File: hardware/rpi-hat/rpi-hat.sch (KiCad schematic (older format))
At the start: 6 parts, among them P1 Conn_02x20_Odd_Even, U1 Telaire_6004_CO2

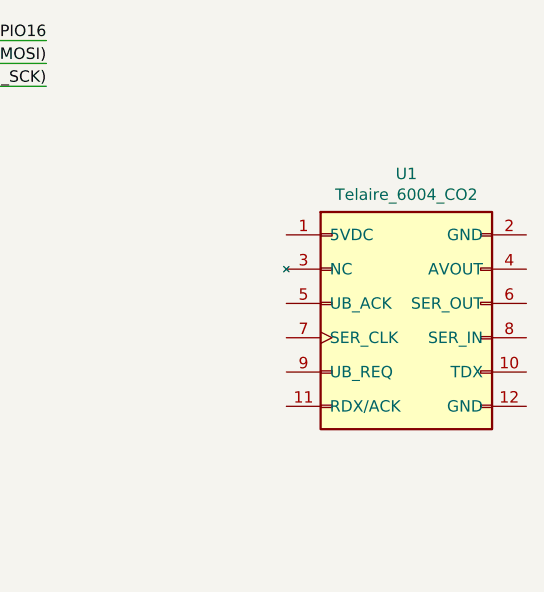
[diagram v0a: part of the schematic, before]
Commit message: Add KiCad Symbol for Sharp GP2Y1010.
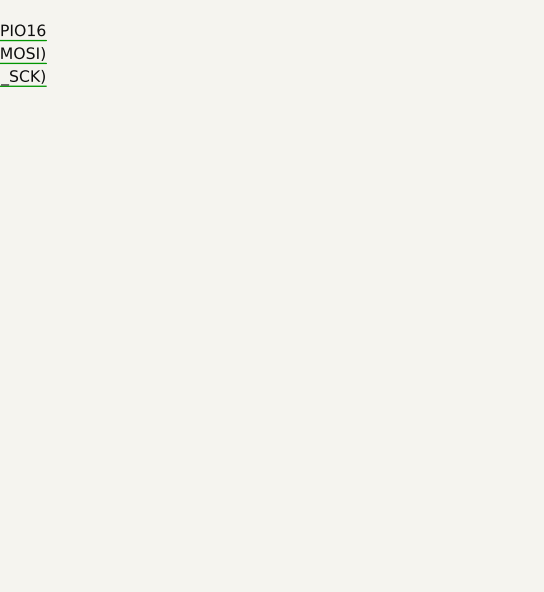
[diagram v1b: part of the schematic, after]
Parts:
- removed U1: Telaire_6004_CO2, symbol zephyrus_iaq:Telaire_6004_CO2
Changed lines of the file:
@@
 Wire Wire Line
 	3000 1700 3000 2000
-$Comp
-L zephyrus_iaq:Telaire_6004_CO2 U1
-U 1 1 5CB19ACF
-P 5150 3550
-F 0 "U1" H 5525 3717 50  0000 C CNN
-F 1 "Telaire_6004_CO2" H 5525 3626 50  0000 C CNN
-F 2 "" H 5700 2400 50  0001 C CNN
-F 3 "" H 5700 2400 50  0001 C CNN
-	1    5150 3550
-	1    0    0    -1
-$EndComp
 $EndSCHEMATC

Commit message: Most functionality added. EEPROM for HAT spec, various JST connectors for sensors, ADC subsystem and power subsystem
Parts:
- added C1: 47uF, Resistor_SMD:R_1206_3216Metric_Pad1.42x1.75mm_HandSolder, symbol Device:C
- added C2: 220uF, Resistor_SMD:R_0805_2012Metric_Pad1.15x1.40mm_HandSolder, symbol Device:CP1_Small
- added D1: SMBJ5.0A, Diode_SMD:D_SMB_Handsoldering, symbol Device:D_Schottky
- added F1: MF-MSMF250/X, Fuse:Fuse_1812_4532Metric, symbol Device:Polyfuse
- added J1: SM04B-SRSS-TB(LF)(SN), symbol zephyrus_iaq:SM04B-SRSS-TB(LF)(SN)
- added J10, J7, J9: S6B-ZR-SM4A-TF(LF)(SN)__Gas, symbol zephyrus_iaq:S6B-ZR-SM4A-TF(LF)(SN)__Gas
- added J2: Conn_01x02_Male, Connector_PinSocket_2.54mm:PinSocket_1x02_P2.54mm_Vertical, symbol Connector:Conn_01x02_Male
- added J3: 10103594-0001LF, 10103594-0001LF:FCI_10103594-0001LF, symbol zephyrus_iaq:10103594-0001LF
- added J4, J6, J8: SM04B-SRSS-TB(LF)(SN), SM04B-SRSS-TB_LF__SN_:JST_SM04B-SRSS-TB(LF)(SN), symbol zephyrus_iaq:SM04B-SRSS-TB(LF)(SN)
- added J5: S6B-ZR-SM4A-TF(LF)(SN)__Dust, symbol zephyrus_iaq:S6B-ZR-SM4A-TF(LF)(SN)__Dust
- added R1: R_US, symbol Device:R_US
- added R2, R3: 3.9k, Resistor_SMD:R_0805_2012Metric_Pad1.15x1.40mm_HandSolder, symbol Device:R_Small_US
- added R4: DNP, Resistor_SMD:R_0805_2012Metric_Pad1.15x1.40mm_HandSolder, symbol Device:R_Small_US
- added R5: 10k, Resistor_SMD:R_0805_2012Metric_Pad1.15x1.40mm_HandSolder, symbol Device:R_Small_US
- added R6: 150, Resistor_SMD:R_0805_2012Metric_Pad1.15x1.40mm_HandSolder, symbol Device:R_Small_US
- added R7: 1700, Resistor_SMD:R_0805_2012Metric_Pad1.15x1.40mm_HandSolder, symbol Device:R_US
- added R8: 3300, Resistor_SMD:R_0805_2012Metric_Pad1.15x1.40mm_HandSolder, symbol Device:R_US
- added U1: CAT24C32WI-GT3, CAT24C32WI-GT3:SOIC127P600X175-8N, symbol zephyrus_iaq:CAT24C32WI-GT3
- added U2: SN74LV4T125PWR, SN74LV4T125PWR:SOP65P640X120-14N, symbol zephyrus_iaq:SN74LV4T125PWR
- added U3: MCP3008T-I_SL, MCP3008T-I_SL:SOIC127P600X175-16N, symbol zephyrus_iaq:MCP3008T-I_SL
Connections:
- net GND is gone; now on net +5V: P1.14 (Pin_14), P1.20 (Pin_20), P1.25 (Pin_25), P1.30 (Pin_30), P1.34 (Pin_34), P1.39 (Pin_39), P1.6 (Pin_6), P1.9 (Pin_9)
- net +3V3: now also J4.3 (3.3V), J6.3 (3.3V), J8.3 (3.3V), R2.1, R3.1, R5.2, U1.8 (VCC)
- net +5V: now also C1.1, C1.2, C2.2, D1.1 (K), D1.2 (A), F1.1, J10.1 (VCC), J10.6 (GND), J2.2 (Pin_2), J3.5, J3.S3 (SHIELD), J3.S4 (SHIELD), J3.S5 (SHIELD), J3.S6 (SHIELD), J4.4 (GND), J5.2 (LED-GND), J5.4 (S-GND), J5.6 (Vcc), J6.4 (GND), J7.1 (VCC), J7.6 (GND), J8.4 (GND), J9.1 (VCC), J9.6 (GND), R4.1, R6.2, R8.2, U1.1 (A0), U1.2 (A1), U1.3 (A2), U1.4 (VSS), U2.1 (1!OE), U2.10 (3!OE), U2.13 (4!OE), U2.14 (VCC), U2.4 (2!OE), U2.7 (GND), U3.14 (AGND), U3.15 (VREF), U3.16 (VDD), U3.9 (DGND); no longer P1.2 (Pin_2), P1.4 (Pin_4)
- net GPIO10(SPI0_MOSI) renamed MOSI_3.3
- net MOSI_3.3: now also U2.5 (2A)
- net GPIO11(SPI0_SCK) renamed SCK_3.3
- net SCK_3.3: now also U2.2 (1A)
- net GPIO14(TXD0) renamed TXD0
- net GPIO15(RXD0) renamed RXD0
- net GPIO18(GEN1)(PWM0) renamed PWM0_3.3
- net PWM0_3.3: now also U2.12 (4A)
- net GPIO2(SDA1) renamed SDA
- net SDA: now also J4.2 (SDA), J6.2 (SDA), J8.2 (SDA)
- net GPIO3(SCL1) renamed SCL
- net SCL: now also J4.1 (SCL), J6.1 (SCL), J8.1 (SCL)
- net GPIO8(SPI0_CE_N) renamed ~CE~_3.3
- net ~CE~_3.3: now also U2.9 (3A)
- net GPIO9(SPI0_MISO) renamed MISO_3.3
- net MISO_3.3: now also R7.2, R8.1
- net ID_SC renamed ID_SC_EEPROM
- net ID_SC_EEPROM: now also R3.2, U1.5 (SDA)
- net ID_SD renamed ID_SD_EEPROM
- net ID_SD_EEPROM: now also R2.2, U1.6 (SCL)
- new net: C2.1, J5.1 (V-LED), R6.1
- new net: R7.1, U3.12 (DOUT)
- new net: J2.1 (Pin_1), R4.2, R5.1, U1.7 (WP)
- new net: F1.2, J3.1
- new net ADC0: J10.2 (A0), J7.2 (A0), J9.2 (A0), U3.1 (CH0)
- new net ADC0_En: J10.4 (En0), J7.4 (En0), J9.4 (En0)
- new net ADC1: J10.3 (A1), J7.3 (A1), J9.3 (A1), U3.2 (CH1)
- new net ADC1_En: J10.5 (En1), J7.5 (En1), J9.5 (En1)
- new net ADC2: U3.3 (CH2)
- new net ADC3: U3.4 (CH3)
- new net ADC4: U3.5 (CH4)
- new net ADC5: U3.6 (CH5)
- new net ADC6: J5.5 (Vo), U3.7 (CH6)
- new net MOSI_5: U2.6 (2Y), U3.11 (DIN)
- new net PWM0_5: J5.3 (LED), U2.11 (4Y)
- new net SCK_5: U2.3 (1Y), U3.13 (CLK)
- new net ~CE~_5: U2.8 (3Y), U3.10 (*CS/SHDN)
- no-connect marks 0 -> 8
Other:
- note added: "3.3V to 5V Logic Conversion"
- note added: "5V Power: Micro USB Input"
- note added: "Analog Connector Ports (MQ Gas Sesnors)"
- note added: "Analog to Digital Converter"
- note added: "BME860 Air Quality"
- note added: "CO2 & Temperature & Humidity Sensor (SCD30)"
- note added: "EEPROM"
- note added: "Pullup Resistors"
- note added: "Sharp GP2Y1010: Dust Sensor"
- note added: "SparkFun GPS Breakout - XA1110 (Qwiic)"

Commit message: Begin layout
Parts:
- removed D1: SMBJ5.0A, Diode_SMD:D_SMB_Handsoldering, symbol Device:D_Schottky
- removed J1: SM04B-SRSS-TB(LF)(SN), symbol zephyrus_iaq:SM04B-SRSS-TB(LF)(SN)
- removed MK1, MK2, MK3, MK4: M2.5, MountingHole:MountingHole_2.7mm_M2.5, symbol rpi-hat-rescue:Mounting_Hole-Mechanical
- removed P1: Conn_02x20_Odd_Even, Connector_PinSocket_2.54mm:PinSocket_2x20_P2.54mm_Vertical, symbol Connector_Generic:Conn_02x20_Odd_Even
- removed R1: R_US, symbol Device:R_US
- added D1: SMBJ5.0A, zephyrus-iaq:SMBJ5.0A, symbol zephyrus_iaq:SMBJ5.0A
- added J1: Conn_02x20_Odd_Even__Rpi, Connector_PinHeader_2.54mm:PinHeader_2x20_P2.54mm_Vertical, symbol zephyrus_iaq:Conn_02x20_Odd_Even__Rpi
- added MK1, MK2, MK3, MK4: M2.5, MountingHole:MountingHole_2.7mm_M2.5, symbol zephyrus_iaq:Mounting-Hole-Mechanical
- J5: footprint (none) -> S6B-ZR-SM4A-TF_LF__SN_:JST_S6B-ZR-SM4A-TF(LF)(SN); symbol zephyrus_iaq:S6B-ZR-SM4A-TF(LF)(SN)__Dust -> rpi-hat-rescue:S6B-ZR-SM4A-TF(LF)(SN)__Dust-zephyrus_iaq
- J6: renamed from J7; footprint (none) -> S6B-ZR-SM4A-TF_LF__SN_:JST_S6B-ZR-SM4A-TF(LF)(SN)
- J7: renamed from J9; footprint (none) -> S6B-ZR-SM4A-TF_LF__SN_:JST_S6B-ZR-SM4A-TF(LF)(SN)
- J8: renamed from J10; footprint (none) -> S6B-ZR-SM4A-TF_LF__SN_:JST_S6B-ZR-SM4A-TF(LF)(SN)
- U2: symbol zephyrus_iaq:SN74LV4T125PWR -> rpi-hat-rescue:SN74LV4T125PWR-zephyrus_iaq
- U3: renamed from U1; symbol zephyrus_iaq:CAT24C32WI-GT3 -> rpi-hat-rescue:CAT24C32WI-GT3-zephyrus_iaq
- renumbered C2 to C1, C1 to C2, J2 to J10, J4 to J2, J6 to J3, J8 to J4, J3 to J9, R6 to R1, R7 to R4, R8 to R6, R4 to R7, U3 to U1
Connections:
- net labels added: ADC2_En, ADC3_En, ADC4_En, ADC5_En
- net labels removed: RXD0, TXD0
- wire segments 141 -> 148
- no-connect marks 8 -> 21
